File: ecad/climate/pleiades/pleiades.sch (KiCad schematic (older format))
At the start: 14 parts, among them J1 MCV 1,5/ 2-G-3,5, J10 47053-1000, J11 47053-1000, J2 MCV 1,5/ 2-G-3,5, J3 MCV 1,5/ 2-G-3,5, J5 47053-1000, J6 47053-1000, J7 215079-8, J8 640454-2, J9 640454-2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

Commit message: Makes Pleiades KiCad 5 compatible
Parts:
- D1, D2: footprint Diodes_SMD:D_MicroMELF -> Diode_SMD:D_MicroMELF; symbol D -> Device:D
- J1, J2, J3: footprint Connectors_Phoenix:PhoenixContact_MCV-G_02x3.50mm_Vertical -> Connector_Phoenix_MC:PhoenixContact_MCV_1,5_2-G-3.5_1x02_P3.50mm_Vertical; symbol Conn_01x02 -> Connector_Generic:Conn_01x02
- J10, J11, J5, J6, J7: symbol Conn_01x04 -> Connector_Generic:Conn_01x04
- J8, J9: symbol Conn_01x02 -> Connector_Generic:Conn_01x02
- Q1, Q2: footprint TO_SOT_Packages_SMD:SOT-23 -> Package_TO_SOT_SMD:SOT-23; symbol Q_NMOS_GSD -> Device:Q_NMOS_GSD
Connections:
- net Fan PWM Controller 2/PWM1: now also J10.4 (Pin_4)
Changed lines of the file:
@@
-EESchema Schematic File Version 2
-LIBS:power
-LIBS:device
-LIBS:switches
-LIBS:relays
-LIBS:motors
-LIBS:transistors
-LIBS:conn
-LIBS:linear
-LIBS:regul
-LIBS:74xx
-LIBS:cmos4000
-LIBS:adc-dac
-LIBS:memory
-LIBS:xilinx
-LIBS:microcontrollers
-LIBS:dsp
-LIBS:microchip
-LIBS:analog_switches
-LIBS:motorola
-LIBS:texas
-LIBS:intel
-LIBS:audio
-LIBS:interface
-LIBS:digital-audio
-LIBS:philips
-LIBS:display
-LIBS:cypress
-LIBS:siliconi
-LIBS:opto
-LIBS:atmel
-LIBS:contrib
-LIBS:valves
-LIBS:fort
-LIBS:Oscillators
-LIBS:nxp
-LIBS:zeus-cache
-EELAYER 25 0
+EESchema Schematic File Version 4
+LIBS:pleiades-cache
+EELAYER 26 0
 EELAYER END
 $Descr A4 11693 8268
@@
 $EndDescr
 $Comp
-L +12V #PWR01
+L power:+12V #PWR01
 U 1 1 5BA4C0F9
 P 1700 1050
@@
 $EndComp
 $Comp
-L +5V #PWR02
+L power:+5V #PWR02
 U 1 1 5BA4C12E
 P 3250 1050
@@
 $EndSheet
 $Comp
-L +3.3V #PWR03
+L pleiades-rescue:+3.3V #PWR03
 U 1 1 5BA4FC58
 P 4900 1050
@@
 $EndSheet
 $Comp
-L Conn_01x04 J5
+L Connector_Generic:Conn_01x04 J5
 U 1 1 5BA5CE4D
 P 10600 4100
@@
 $EndComp
 $Comp
-L Conn_01x04 J6
+L Connector_Generic:Conn_01x04 J6
 U 1 1 5BA5DACF
 P 10600 4700
@@
 $EndComp
 $Comp
-L +12V #PWR04
+L power:+12V #PWR04
 U 1 1 5BA5E50B
 P 10200 3900
@@
 $EndComp
 $Comp
-L Q_NMOS_GSD Q1
+L Device:Q_NMOS_GSD Q1
 U 1 1 5BA50932
 P 9000 1800
 F 0 "Q1" H 9200 1850 50  0000 L CNN
 F 1 "PMV45EN" H 9200 1750 50  0000 L CNN
-F 2 "TO_SOT_Packages_SMD:SOT-23" H 9200 1900 50  0001 C CNN
+F 2 "Package_TO_SOT_SMD:SOT-23" H 9200 1900 50  0001 C CNN
 F 3 "" H 9000 1800 50  0001 C CNN
 F 4 "PMV45EN" H 9000 1800 60  0001 C CNN "Part Number"
@@
 $EndComp
 $Comp
-L Conn_01x02 J8
+L Connector_Generic:Conn_01x02 J8
 U 1 1 5BA51183
 P 10500 1450
@@
 $EndComp
 $Comp
-L Conn_01x02 J9
+L Connector_Generic:Conn_01x02 J9
 U 1 1 5BA51439
 P 10500 1850
@@
 $EndComp
 $Comp
-L D D2
+L Device:D D2
 U 1 1 5BA51C44
 P 9900 1200
 F 0 "D2" H 9900 1300 50  0000 C CNN
 F 1 "MCL4148" H 9900 1100 50  0000 C CNN
-F 2 "Diodes_SMD:D_MicroMELF" H 9900 1200 50  0001 C CNN
+F 2 "Diode_SMD:D_MicroMELF" H 9900 1200 50  0001 C CNN
 F 3 "" H 9900 1200 50  0001 C CNN
 F 4 "MCL4148-TR" H 9900 1200 60  0001 C CNN "Part Number"
@@
 $EndComp
 $Comp
-L +12V #PWR05
+L power:+12V #PWR05
 U 1 1 5BA521BB
 P 10150 700
@@
 $EndComp
 $Comp
-L D D1
+L Device:D D1
 U 1 1 5BA525E7
 P 9600 1200
 F 0 "D1" H 9600 1300 50  0000 C CNN
 F 1 "MCL4148" H 9600 1100 50  0000 C CNN
-F 2 "Diodes_SMD:D_MicroMELF" H 9600 1200 50  0001 C CNN
+F 2 "Diode_SMD:D_MicroMELF" H 9600 1200 50  0001 C CNN
 F 3 "" H 9600 1200 50  0001 C CNN
 F 4 "MCL4148-TR" H 9600 1200 60  0001 C CNN "Part Number"
@@
 $EndComp
 $Comp
-L Q_NMOS_GSD Q2
+L Device:Q_NMOS_GSD Q2
 U 1 1 5BA52B10
 P 9350 2250
 F 0 "Q2" H 9550 2300 50  0000 L CNN
 F 1 "PMV45EN" H 9550 2200 50  0000 L CNN
-F 2 "TO_SOT_Packages_SMD:SOT-23" H 9550 2350 50  0001 C CNN
+F 2 "Package_TO_SOT_SMD:SOT-23" H 9550 2350 50  0001 C CNN
 F 3 "" H 9350 2250 50  0001 C CNN
 F 4 "PMV45EN" H 9350 2250 60  0001 C CNN "Part Number"
@@
 $EndComp
 $Comp
-L GND #PWR06
+L power:GND #PWR06
 U 1 1 5BA52C82
 P 9100 2050
@@
 $EndComp
 $Comp
-L GND #PWR07
+L power:GND #PWR07
 U 1 1 5BA52E0E
 P 9450 2500
@@
 PC 4 Wire Fans
 $Comp
-L Conn_01x02 J2
+L Connector_Generic:Conn_01x02 J2
 U 1 1 5BA55E48
 P 700 4500
 F 0 "J2" H 700 4600 50  0000 C CNN
 F 1 "MCV 1,5/ 2-G-3,5" H 700 4300 50  0000 C CNN
-F 2 "Connectors_Phoenix:PhoenixContact_MCV-G_02x3.50mm_Vertical" H 700 4500 50  0001 C CNN
+F 2 "Connector_Phoenix_MC:PhoenixContact_MCV_1,5_2-G-3.5_1x02_P3.50mm_Vertical" H 700 4500 50  0001 C CNN
 F 3 "" H 700 4500 50  0001 C CNN
 F 4 "MCV 1,5/ 2-G-3,5" H 700 4500 60  0001 C CNN "Part Number"
@@
 $EndComp
 $Comp
-L Conn_01x02 J1
+L Connector_Generic:Conn_01x02 J1
 U 1 1 5BA560A5
 P 700 4050
 F 0 "J1" H 700 4150 50  0000 C CNN
 F 1 "MCV 1,5/ 2-G-3,5" H 700 3850 50  0000 C CNN
-F 2 "Connectors_Phoenix:PhoenixContact_MCV-G_02x3.50mm_Vertical" H 700 4050 50  0001 C CNN
+F 2 "Connector_Phoenix_MC:PhoenixContact_MCV_1,5_2-G-3.5_1x02_P3.50mm_Vertical" H 700 4050 50  0001 C CNN
 F 3 "" H 700 4050 50  0001 C CNN
 F 4 "MCV 1,5/ 2-G-3,5" H 700 4050 60  0001 C CNN "Part Number"
@@
 $EndComp
 $Comp
-L Conn_01x02 J3
+L Connector_Generic:Conn_01x02 J3
 U 1 1 5BA567FD
 P 1050 1300
 F 0 "J3" H 1050 1400 50  0000 C CNN
 F 1 "MCV 1,5/ 2-G-3,5" H 1050 1100 50  0000 C CNN
-F 2 "Connectors_Phoenix:PhoenixContact_MCV-G_02x3.50mm_Vertical" H 1050 1300 50  0001 C CNN
+F 2 "Connector_Phoenix_MC:PhoenixContact_MCV_1,5_2-G-3.5_1x02_P3.50mm_Vertical" H 1050 1300 50  0001 C CNN
 F 3 "" H 1050 1300 50  0001 C CNN
 F 4 "MCV 1,5/ 2-G-3,5" H 1050 1300 60  0001 C CNN "Part Number"
@@
 $EndComp
 $Comp
-L GND #PWR08
+L power:GND #PWR08
 U 1 1 5BA570D8
 P 1500 1600
@@
 HEAT2_PWR
 $Comp
-L Conn_01x04 J7
+L Connector_Generic:Conn_01x04 J7
 U 1 1 5BA66436
 P 10600 3150
@@
 $EndComp
 $Comp
-L +3.3V #PWR09
+L pleiades-rescue:+3.3V #PWR09
 U 1 1 5BA662B5
 P 10200 2900
@@
 $EndComp
 $Comp
-L GND #PWR010
+L power:GND #PWR010
 U 1 1 5BA664CF
 P 10200 3500
@@
 $EndSheet
 $Comp
-L Conn_01x04 J10
+L Connector_Generic:Conn_01x04 J10
 U 1 1 5BAA7145
 P 10600 5300
@@
 $EndComp
 $Comp
-L Conn_01x04 J11
+L Connector_Generic:Conn_01x04 J11
 U 1 1 5BAA714C
 P 10600 5900
@@
 $EndComp
 $Comp
-L GND #PWR011
+L power:GND #PWR011
 U 1 1 5BAA7152
 P 10300 6250
@@
 	1700 1050 1700 1300
 Wire Wire Line
-	1250 1300 1850 1300
-Wire Wire Line
-	3000 1300 3500 1300
+	1250 1300 1700 1300
+Wire Wire Line
+	3000 1300 3250 1300
 Wire Wire Line
 	3250 1300 3250 1050
@@
 	9800 4800 10400 4800
 Wire Wire Line
-	10150 700  10150 1850
+	10150 700  10150 800
 Wire Wire Line
 	10150 1450 10300 1450
@@
 	9900 1350 9900 1550
 Wire Wire Line
-	9100 1550 10300 1550
+	9100 1550 9900 1550
 Wire Wire Line
 	9900 1050 9900 800
 Wire Wire Line
-	9600 800  10150 800
+	9600 800  9900 800
 Connection ~ 10150 800
 Wire Wire Line
@@
 	9600 1350 9600 1950
 Wire Wire Line
-	9450 1950 10300 1950
+	9450 1950 9600 1950
 Wire Wire Line
 	9100 1550 9100 1600
@@
 	9100 2050 9100 2000
 Wire Wire Line
-	900  4050 1550 4050
-Wire Wire Line
-	900  4150 1550 4150
+	900  4050 1200 4050
+Wire Wire Line
+	900  4150 1300 4150
 Wire Wire Line
 	1200 4050 1200 4500
@@
 Connection ~ 10200 5300
 Wire Wire Line
-	10200 3900 10200 5900
-Wire Wire Line
-	10300 6250 10300 4000
+	10200 3900 10200 4100
+Wire Wire Line
+	10300 6250 10300 5800
 Wire Wire Line
 	10200 2900 10200 3050
@@
 Wire Wire Line
 	7600 5700 8500 5700
+Wire Wire Line
+	3250 1300 3500 1300
+Wire Wire Line
+	10200 4100 10200 4700
+Wire Wire Line
+	10150 1450 10150 1850
+Wire Wire Line
+	10150 800  10150 1450
+Wire Wire Line
+	9900 800  10150 800
+Wire Wire Line
+	9900 1550 10300 1550
+Wire Wire Line
+	9600 1950 10300 1950
+Wire Wire Line
+	1200 4050 1550 4050
+Wire Wire Line
+	1300 4150 1550 4150
+Wire Wire Line
+	1700 1300 1850 1300
+Wire Wire Line
+	10300 5800 10300 5200
+Wire Wire Line
+	10300 5200 10300 4600
+Wire Wire Line
+	10300 4600 10300 4000
+Wire Wire Line
+	10200 4700 10200 5300
+Wire Wire Line
+	10200 5300 10200 5900
+Wire Wire Line
+	9500 5500 10400 5500
 $EndSCHEMATC

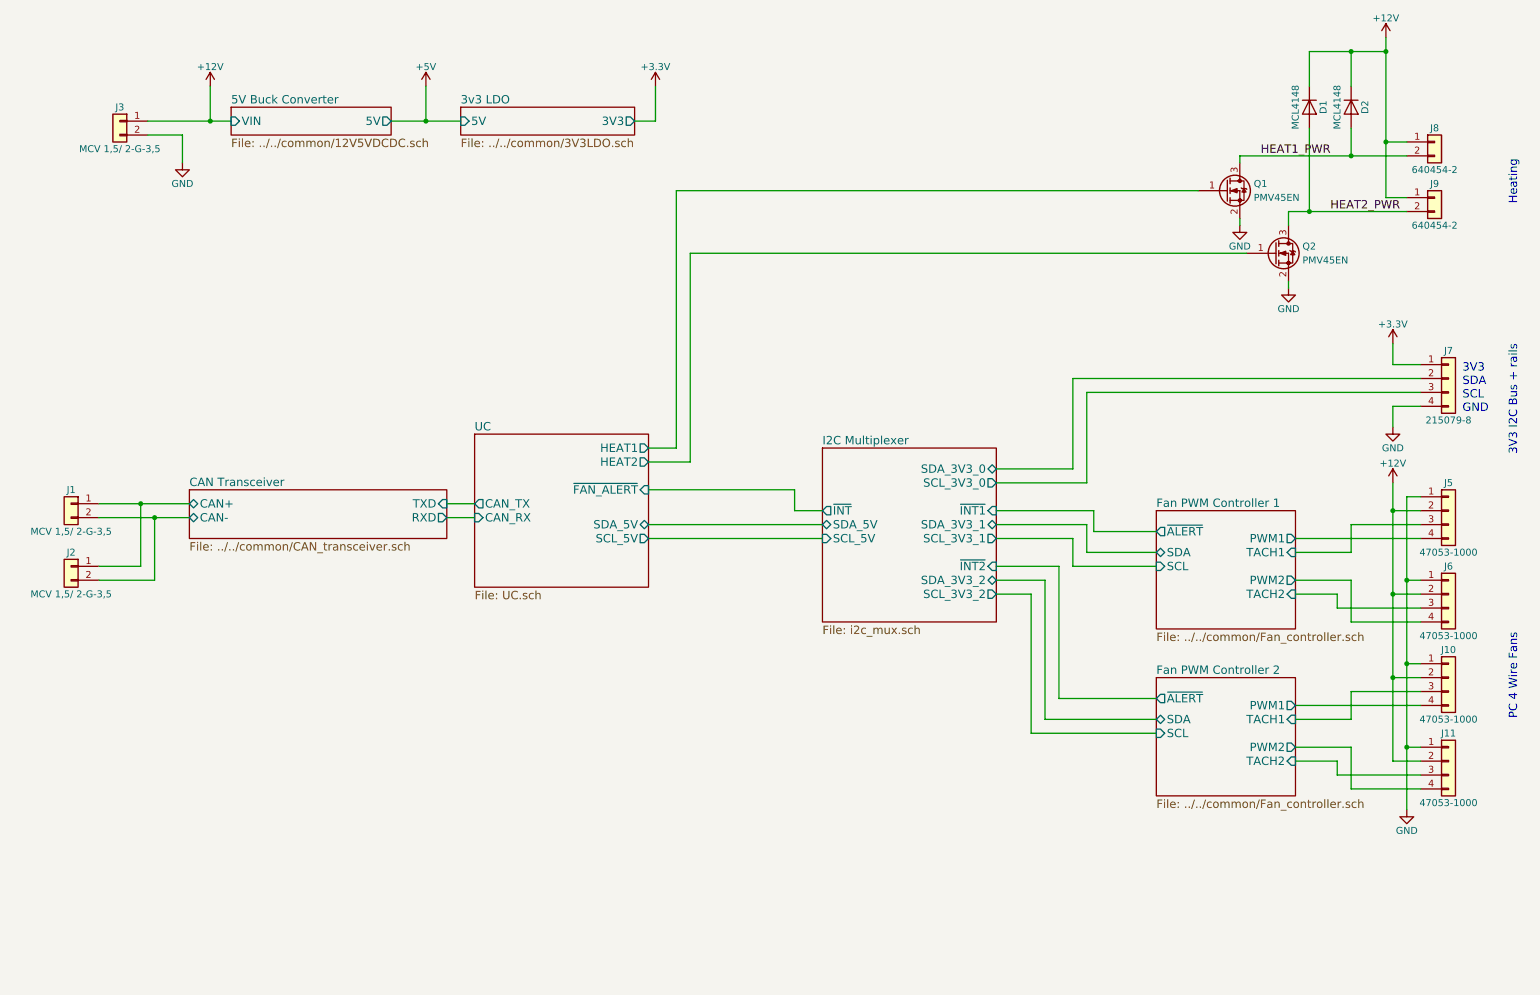
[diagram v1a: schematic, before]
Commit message: Makes one board that fit them all
Bad Idea, will revert the changes soon
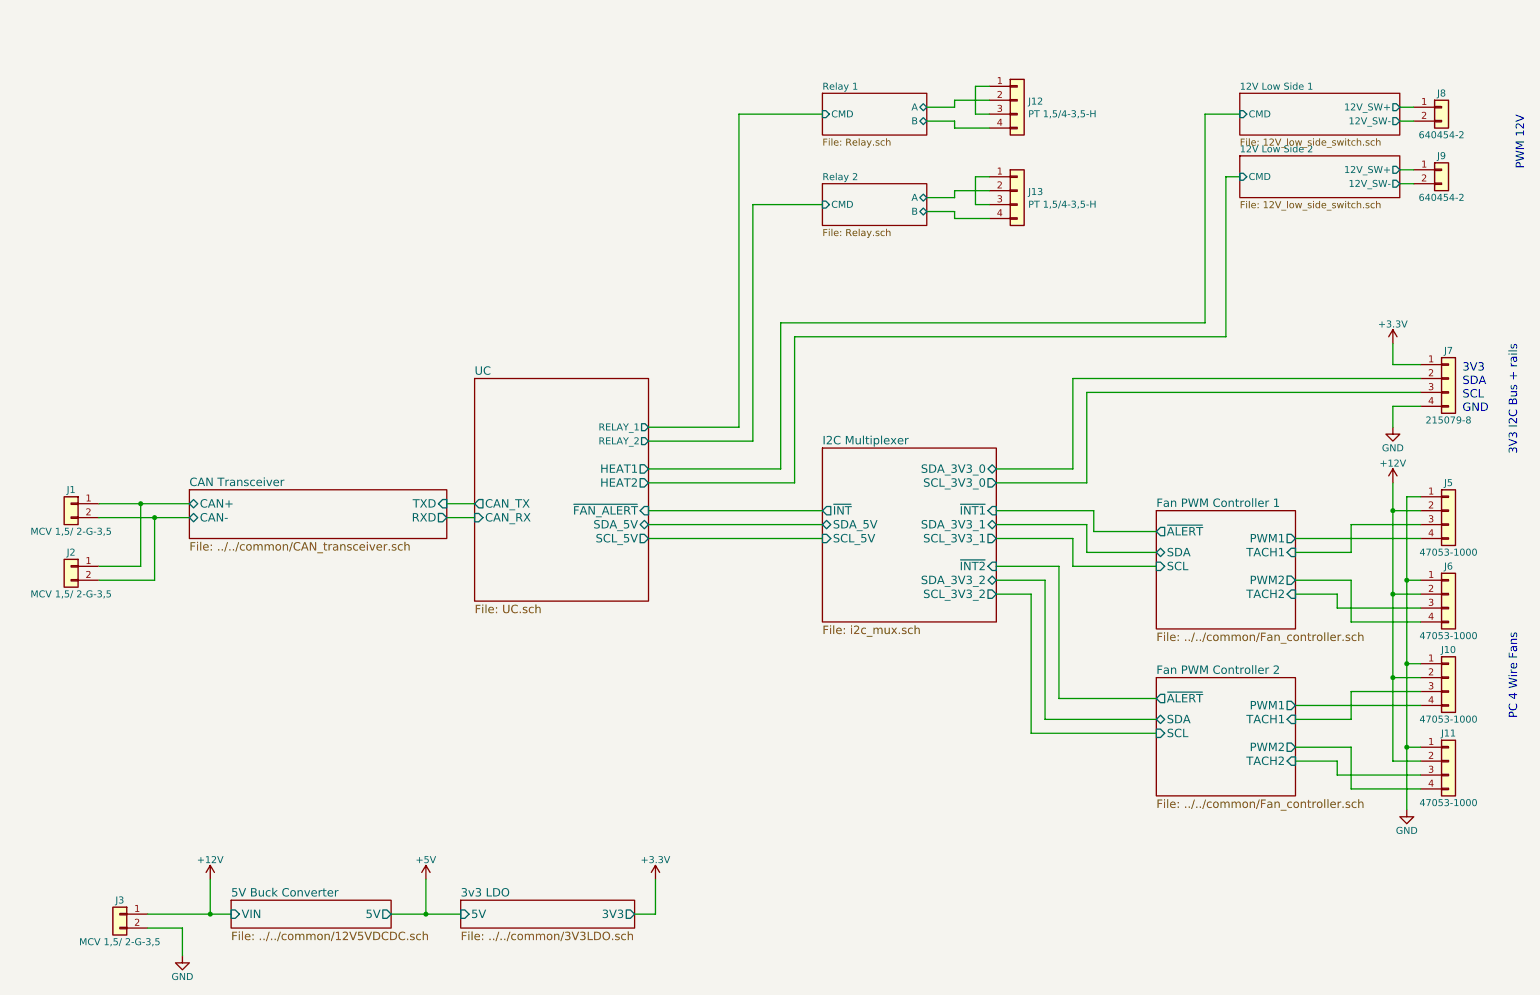
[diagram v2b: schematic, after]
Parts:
- removed D1, D2: MCL4148, Diode_SMD:D_MicroMELF, symbol Device:D
- removed Q1, Q2: PMV45EN, Package_TO_SOT_SMD:SOT-23, symbol Device:Q_NMOS_GSD
- added J12, J13: PT 1,5/4-3,5-H, TerminalBlock_Phoenix:TerminalBlock_Phoenix_PT-1,5-4-3.5-H_1x04_P3.50mm_Horizontal, symbol Connector_Generic:Conn_01x04
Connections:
- net +12V: no longer J8.1 (Pin_1), J9.1 (Pin_1)
- net HEAT1_PWR renamed 12V Low Side 1/12V_SW-
- net HEAT2_PWR renamed 12V Low Side 2/12V_SW-
- new net: J12.1 (Pin_1), J12.3 (Pin_3)
- new net: J13.1 (Pin_1), J13.3 (Pin_3)
- new net 12V Low Side 1/12V_SW+: J8.1 (Pin_1)
- new net 12V Low Side 2/12V_SW+: J9.1 (Pin_1)
- new net Relay 1/A: J12.2 (Pin_2)
- new net Relay 1/B: J12.4 (Pin_4)
- new net Relay 2/A: J13.2 (Pin_2)
- new net Relay 2/B: J13.4 (Pin_4)
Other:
- note added: "PWM 12V"
- note removed: "Heating"
- moved on the sheet: J3, J8, J9
